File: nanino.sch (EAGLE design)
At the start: 19 parts, among them IC1 ATMEGA168-20P

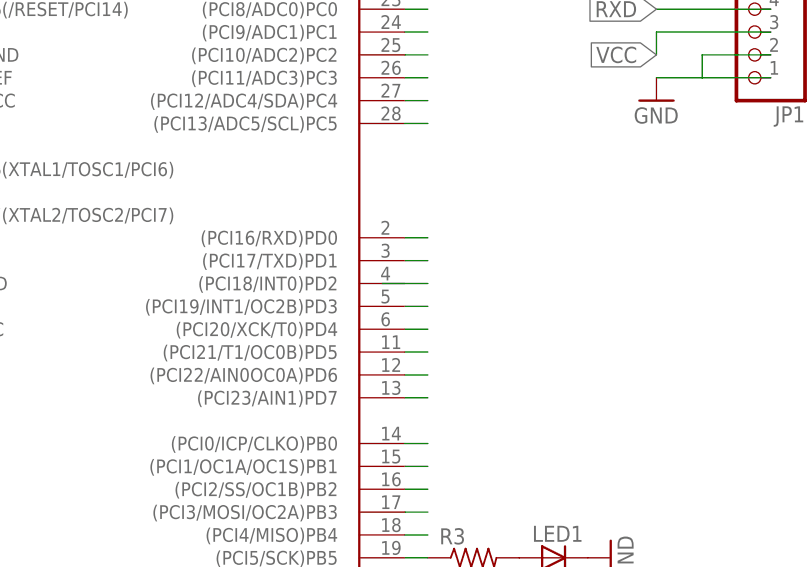
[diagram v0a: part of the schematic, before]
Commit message: Added missing D2 Pin
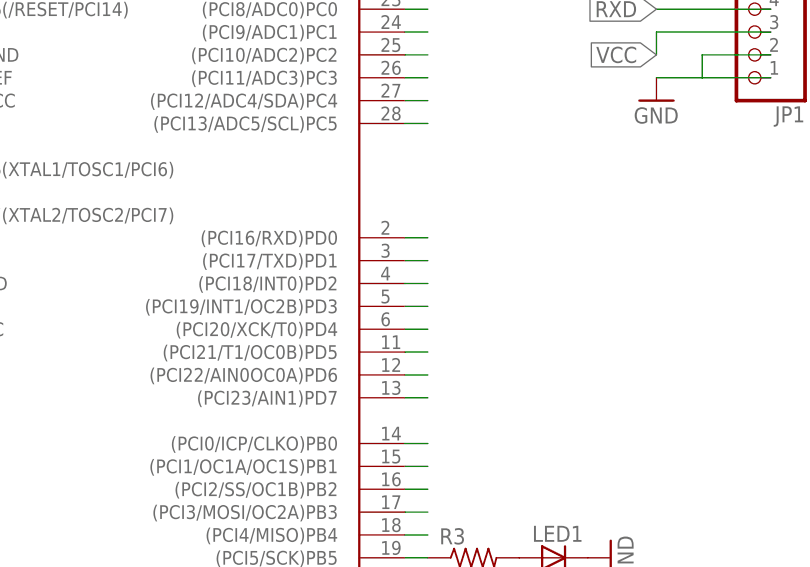
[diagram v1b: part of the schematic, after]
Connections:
- net D2: now also IC1.(PCI18/INT0)PD2
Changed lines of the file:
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@@
 </segment>
 <segment>
-<wire x1="165.1" y1="53.34" x2="170.18" y2="53.34" width="0.1524" layer="91"/>
+<pinref part="IC1" gate="G$1" pin="(PCI18/INT0)PD2"/>
+<wire x1="167.64" y1="53.34" x2="170.18" y2="53.34" width="0.1524" layer="91"/>
 </segment>
 </net>

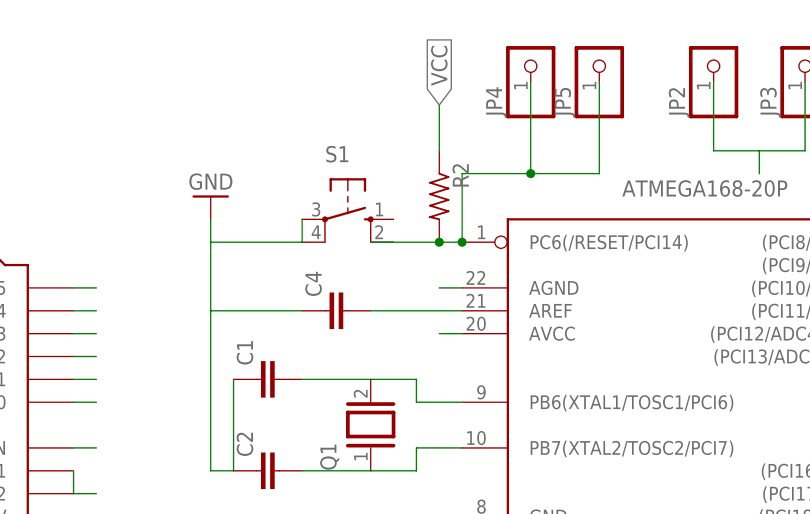
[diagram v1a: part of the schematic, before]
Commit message: Fixed Reset Button Wire
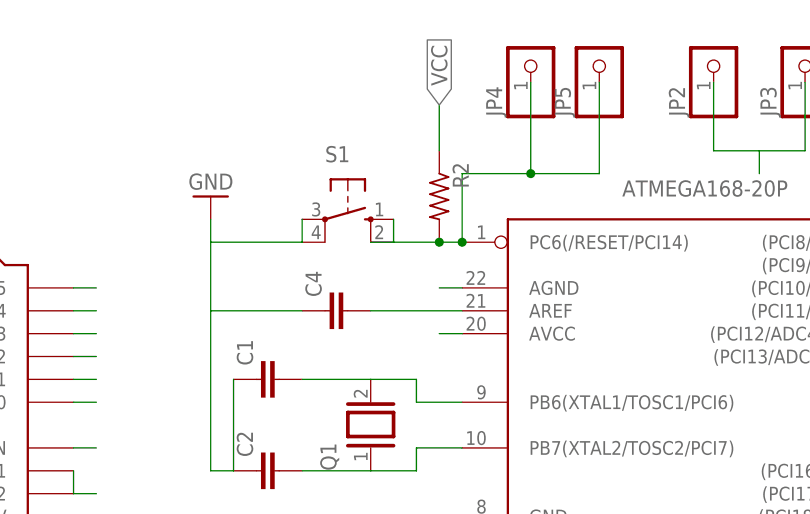
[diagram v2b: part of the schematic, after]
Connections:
- net RESET: now also S1.S
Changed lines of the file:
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@@
 <wire x1="111.76" y1="83.82" x2="109.22" y2="83.82" width="0.1524" layer="91"/>
 <pinref part="R2" gate="G$1" pin="2"/>
-<wire x1="109.22" y1="83.82" x2="101.6" y2="83.82" width="0.1524" layer="91"/>
+<wire x1="109.22" y1="83.82" x2="104.14" y2="83.82" width="0.1524" layer="91"/>
 <junction x="109.22" y="83.82"/>
+<wire x1="104.14" y1="83.82" x2="101.6" y2="83.82" width="0.1524" layer="91"/>
 <wire x1="127" y1="91.44" x2="119.38" y2="91.44" width="0.1524" layer="91"/>
 <wire x1="119.38" y1="91.44" x2="111.76" y2="91.44" width="0.1524" layer="91"/>
@@
 <pinref part="JP5" gate="G$1" pin="1"/>
 <wire x1="127" y1="101.6" x2="127" y2="91.44" width="0.1524" layer="91"/>
+<pinref part="S1" gate="1" pin="S"/>
+<wire x1="104.14" y1="86.36" x2="104.14" y2="83.82" width="0.1524" layer="91"/>
 </segment>
 <segment>
